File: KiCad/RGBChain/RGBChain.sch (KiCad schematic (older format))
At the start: 72 parts, among them J1 AudioJack2_Ground, J2 SWD, J3 USB_B_Micro, J4 Barrel_Jack, P1 USB_C_Plug_USB2.0, Q1 IRF7404, Q2 SQJB80EP, Q3 IRLML2502, SW1 Rotary_Encoder_Switch, SW2 SW_SPDT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

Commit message: PCB done
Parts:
- removed D6: WS2812B, LED_THT:LED_D5.0mm-4_RGB_Staggered_Pins, symbol LED:WS2812B
- added D6: WS2812D, LED_THT:LED_D5.0mm-4_RGB, symbol myLib:WS2812D
- added D7, D8: RED LED, LED_THT:LED_D3.0mm, symbol Device:LED
- J1: footprint Connector_Audio:Jack_3.5mm_CUI_SJ-3523-SMT_Horizontal -> JPConnectors:Jack_3.5mm_Lumberg_1503_03
- SW2: footprint Button_Switch_THT:SW_E-Switch_EG1224_SPDT_Angled -> JPSwitches:NINIGI_5F_M6
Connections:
- wire segments 224 -> 238
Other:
- note added: "I(d)=16mA*3=48mA"
- moved on the sheet: D3, R1
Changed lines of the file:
@@
 $EndDescr
-$Comp
-L LED:WS2812B D6
-U 1 1 5F8AD20A
-P 14700 4200
-F 0 "D6" H 15044 4246 50  0000 L CNN
-F 1 "WS2812B" H 15044 4155 50  0000 L CNN
-F 2 "LED_THT:LED_D5.0mm-4_RGB_Staggered_Pins" H 14750 3900 50  0001 L TNN
-F 3 "https://cdn-shop.adafruit.com/datasheets/WS2812B.pdf" H 14800 3825 50  0001 L TNN
-	1    14700 4200
-	1    0    0    -1
-$EndComp
 $Comp
 L Device:Battery_Cell BT1
@@
 F 0 "J1" H 14470 3168 50  0000 R CNN
 F 1 "AudioJack2_Ground" H 14470 3077 50  0000 R CNN
-F 2 "Connector_Audio:Jack_3.5mm_CUI_SJ-3523-SMT_Horizontal" H 14650 3150 50  0001 C CNN
+F 2 "JPConnectors:Jack_3.5mm_Lumberg_1503_03" H 14650 3150 50  0001 C CNN
 F 3 "~" H 14650 3150 50  0001 C CNN
 	1    14650 3150
@@
 U 1 1 5F8C9FC5
 P 3650 4150
-F 0 "D2" V 3689 4032 50  0000 R CNN
-F 1 "RED LED" V 3598 4032 50  0000 R CNN
+F 0 "D2" V 3700 4350 50  0000 R CNN
+F 1 "RED LED" V 3600 4550 50  0000 R CNN
 F 2 "LED_SMD:LED_0805_2012Metric" H 3650 4150 50  0001 C CNN
 F 3 "~" H 3650 4150 50  0001 C CNN
@@
 L Device:R R1
 U 1 1 5F8CA8EE
-P 3650 4450
-F 0 "R1" H 3580 4404 50  0000 R CNN
-F 1 "3k3" H 3580 4495 50  0000 R CNN
-F 2 "Resistor_SMD:R_0805_2012Metric" V 3580 4450 50  0001 C CNN
-F 3 "~" H 3650 4450 50  0001 C CNN
-	1    3650 4450
+P 3650 4550
+F 0 "R1" H 3580 4504 50  0000 R CNN
+F 1 "3k3" H 3580 4595 50  0000 R CNN
+F 2 "Resistor_SMD:R_0805_2012Metric" V 3580 4550 50  0001 C CNN
+F 3 "~" H 3650 4550 50  0001 C CNN
+	1    3650 4550
 	-1   0    0    1
 $EndComp
@@
 Connection ~ 3650 3900
 Wire Wire Line
-	3650 3900 4200 3900
+	3650 3900 3800 3900
 $Comp
 L power:VBUS #PWR0103
@@
 L power:GNDPWR #PWR0104
 U 1 1 5F8D62DF
-P 3650 4600
-F 0 "#PWR0104" H 3650 4400 50  0001 C CNN
-F 1 "GNDPWR" H 3654 4446 50  0000 C CNN
-F 2 "" H 3650 4550 50  0001 C CNN
-F 3 "" H 3650 4550 50  0001 C CNN
-	1    3650 4600
+P 3650 4700
+F 0 "#PWR0104" H 3650 4500 50  0001 C CNN
+F 1 "GNDPWR" H 3654 4546 50  0000 C CNN
+F 2 "" H 3650 4650 50  0001 C CNN
+F 3 "" H 3650 4650 50  0001 C CNN
+	1    3650 4700
 	1    0    0    -1
 $EndComp
@@
 L Device:LED D3
 U 1 1 5F8DB333
-P 6400 4800
-F 0 "D3" H 6393 5016 50  0000 C CNN
-F 1 "RED LED" H 6393 4925 50  0000 C CNN
-F 2 "LED_SMD:LED_0805_2012Metric" H 6400 4800 50  0001 C CNN
-F 3 "~" H 6400 4800 50  0001 C CNN
-	1    6400 4800
+P 6500 4800
+F 0 "D3" H 6500 4550 50  0000 C CNN
+F 1 "RED LED" H 6500 4650 50  0000 C CNN
+F 2 "LED_SMD:LED_0805_2012Metric" H 6500 4800 50  0001 C CNN
+F 3 "~" H 6500 4800 50  0001 C CNN
+	1    6500 4800
 	1    0    0    -1
 $EndComp
@@
 L power:VBUS #PWR0108
 U 1 1 5F8DBA77
-P 6550 4800
-F 0 "#PWR0108" H 6550 4650 50  0001 C CNN
-F 1 "VBUS" V 6565 4928 50  0000 L CNN
-F 2 "" H 6550 4800 50  0001 C CNN
-F 3 "" H 6550 4800 50  0001 C CNN
-	1    6550 4800
+P 6750 4800
+F 0 "#PWR0108" H 6750 4650 50  0001 C CNN
+F 1 "VBUS" V 6765 4928 50  0000 L CNN
+F 2 "" H 6750 4800 50  0001 C CNN
+F 3 "" H 6750 4800 50  0001 C CNN
+	1    6750 4800
 	0    1    1    0
 $EndComp
@@
 F 0 "SW2" H 2000 6535 50  0000 C CNN
 F 1 "SW_SPDT" H 2000 6444 50  0000 C CNN
-F 2 "Button_Switch_THT:SW_E-Switch_EG1224_SPDT_Angled" H 2000 6250 50  0001 C CNN
+F 2 "JPSwitches:NINIGI_5F_M6" H 2000 6250 50  0001 C CNN
 F 3 "~" H 2000 6250 50  0001 C CNN
 	1    2000 6250
@@
 Wire Wire Line
 	11600 6000 11450 6000
+$Comp
+L Device:LED D7
+U 1 1 5FF899B0
+P 3800 4150
+F 0 "D7" V 3839 4032 50  0000 R CNN
+F 1 "RED LED" V 3748 4032 50  0000 R CNN
+F 2 "LED_THT:LED_D3.0mm" H 3800 4150 50  0001 C CNN
+F 3 "~" H 3800 4150 50  0001 C CNN
+	1    3800 4150
+	0    -1   -1   0
+$EndComp
+Wire Wire Line
+	3650 4300 3650 4350
+Wire Wire Line
+	3650 4350 3800 4350
+Wire Wire Line
+	3800 4350 3800 4300
+Connection ~ 3650 4350
+Wire Wire Line
+	3650 4350 3650 4400
+Wire Wire Line
+	3800 4000 3800 3900
+Connection ~ 3800 3900
+Wire Wire Line
+	3800 3900 4200 3900
+$Comp
+L Device:LED D8
+U 1 1 5FFDB156
+P 6500 4650
+F 0 "D8" H 6493 4866 50  0000 C CNN
+F 1 "RED LED" H 6493 4775 50  0000 C CNN
+F 2 "LED_THT:LED_D3.0mm" H 6500 4650 50  0001 C CNN
+F 3 "~" H 6500 4650 50  0001 C CNN
+	1    6500 4650
+	1    0    0    -1
+$EndComp
+Wire Wire Line
+	6250 4800 6300 4800
+Wire Wire Line
+	6300 4800 6300 4650
+Wire Wire Line
+	6300 4650 6350 4650
+Connection ~ 6300 4800
+Wire Wire Line
+	6300 4800 6350 4800
+Wire Wire Line
+	6650 4650 6700 4650
+Wire Wire Line
+	6700 4650 6700 4800
+Wire Wire Line
+	6700 4800 6650 4800
+Wire Wire Line
+	6700 4800 6750 4800
+Connection ~ 6700 4800
+Text Notes 14600 4850 0    50   ~ 0
+I(d)=16mA*3=48mA
+$Comp
+L myLib:WS2812D D6
+U 1 1 6008788C
+P 14700 4200
+F 0 "D6" H 15044 4246 50  0000 L CNN
+F 1 "WS2812D" H 15044 4155 50  0000 L CNN
+F 2 "LED_THT:LED_D5.0mm-4_RGB" H 14750 3900 50  0001 L TNN
+F 3 "https://cdn-shop.adafruit.com/datasheets/WS2812B.pdf" H 14800 3825 50  0001 L TNN
+	1    14700 4200
+	1    0    0    -1
+$EndComp
 $EndSCHEMATC

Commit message: PCB more work
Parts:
- removed JP1: 0, Jumper:SolderJumper-2_P1.3mm_Bridged_Pad1.0x1.5mm, symbol Device:Jumper_NC_Small
- BT1, BT2, BT3: footprint Battery:BatteryHolder_Keystone_1042_1x18650 -> JPConnectors:BatteryHolder_Keystone_1042_1x18650
- R10, R4: footprint Resistor_SMD:R_0805_2012Metric -> Resistor_SMD:R_0603_1608Metric
- U5: value STM32L051K8Tx -> STM32L051K8T6
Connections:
- wire segments 238 -> 242
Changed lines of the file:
@@
 F 0 "BT1" H 3200 1650 50  0000 L CNN
 F 1 "Li-Ion" H 2900 1850 50  0000 L CNN
-F 2 "Battery:BatteryHolder_Keystone_1042_1x18650" V 3150 1760 50  0001 C CNN
+F 2 "JPConnectors:BatteryHolder_Keystone_1042_1x18650" V 3150 1760 50  0001 C CNN
 F 3 "~" V 3150 1760 50  0001 C CNN
 	1    3150 1700
@@
 F 0 "BT2" H 3550 1650 50  0000 L CNN
 F 1 "Li-Ion" H 3250 1850 50  0000 L CNN
-F 2 "Battery:BatteryHolder_Keystone_1042_1x18650" V 3500 1760 50  0001 C CNN
+F 2 "JPConnectors:BatteryHolder_Keystone_1042_1x18650" V 3500 1760 50  0001 C CNN
 F 3 "~" V 3500 1760 50  0001 C CNN
 	1    3500 1700
@@
 F 0 "BT3" H 3900 1650 50  0000 L CNN
 F 1 "Li-Ion" H 3600 1850 50  0000 L CNN
-F 2 "Battery:BatteryHolder_Keystone_1042_1x18650" V 3850 1760 50  0001 C CNN
+F 2 "JPConnectors:BatteryHolder_Keystone_1042_1x18650" V 3850 1760 50  0001 C CNN
 F 3 "~" V 3850 1760 50  0001 C CNN
 	1    3850 1700
@@
 F 0 "R4" V 4493 4950 50  0000 C CNN
 F 1 "100k" V 4584 4950 50  0000 C CNN
-F 2 "Resistor_SMD:R_0805_2012Metric" V 4630 4950 50  0001 C CNN
+F 2 "Resistor_SMD:R_0603_1608Metric" V 4630 4950 50  0001 C CNN
 F 3 "~" H 4700 4950 50  0001 C CNN
 	1    4700 4950
@@
 	2250 7650 2250 7500
 $Comp
-L Device:Jumper_NC_Small JP1
-U 1 1 5F8F644E
-P 1750 8150
-F 0 "JP1" H 1750 8362 50  0000 C CNN
-F 1 "0" H 1750 8271 50  0000 C CNN
-F 2 "Jumper:SolderJumper-2_P1.3mm_Bridged_Pad1.0x1.5mm" H 1750 8150 50  0001 C CNN
-F 3 "~" H 1750 8150 50  0001 C CNN
-	1    1750 8150
-	1    0    0    -1
-$EndComp
-$Comp
 L power:GNDPWR #PWR0116
 U 1 1 5F8F6DD7
@@
 L power:GND #PWR0117
 U 1 1 5F8F777D
-P 1850 8150
-F 0 "#PWR0117" H 1850 7900 50  0001 C CNN
-F 1 "GND" V 1855 8022 50  0000 R CNN
-F 2 "" H 1850 8150 50  0001 C CNN
-F 3 "" H 1850 8150 50  0001 C CNN
-	1    1850 8150
+P 1650 8150
+F 0 "#PWR0117" H 1650 7900 50  0001 C CNN
+F 1 "GND" V 1655 8022 50  0000 R CNN
+F 2 "" H 1650 8150 50  0001 C CNN
+F 3 "" H 1650 8150 50  0001 C CNN
+	1    1650 8150
 	0    -1   -1   0
 $EndComp
-Wire Wire Line
-	1750 7500 1750 7650
 $Comp
 L Device:C C13
@@
 F 0 "R10" H 13420 4396 50  0000 L CNN
 F 1 "100k" H 13420 4305 50  0000 L CNN
-F 2 "Resistor_SMD:R_0805_2012Metric" V 13280 4350 50  0001 C CNN
+F 2 "Resistor_SMD:R_0603_1608Metric" V 13280 4350 50  0001 C CNN
 F 3 "~" H 13350 4350 50  0001 C CNN
 	1    13350 4350
@@
 P 10950 5200
 F 0 "U5" H 11050 4100 50  0000 C CNN
-F 1 "STM32L051K8Tx" H 11300 4200 50  0000 C CNN
+F 1 "STM32L051K8T6" H 11300 4200 50  0000 C CNN
 F 2 "Package_QFP:LQFP-32_7x7mm_P0.8mm" H 10450 4300 50  0001 R CNN
 F 3 "http://www.st.com/st-web-ui/static/active/en/resource/technical/document/datasheet/DM00108219.pdf" H 10950 5200 50  0001 C CNN
@@
 	1    0    0    -1
 $EndComp
+Wire Wire Line
+	1700 7500 1700 7550
+Wire Wire Line
+	1700 7550 1750 7550
+Wire Wire Line
+	1800 7550 1800 7500
+Wire Wire Line
+	1750 7650 1750 7550
+Connection ~ 1750 7550
+Wire Wire Line
+	1750 7550 1800 7550
 $EndSCHEMATC

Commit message: Last pcb changes
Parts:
- removed J2: SWD, Connector_PinHeader_2.54mm:PinHeader_1x06_P2.54mm_Vertical, symbol Connector_Generic:Conn_01x06
- added J2: SWD, Connector_PinHeader_2.54mm:PinHeader_1x05_P2.54mm_Vertical, symbol Connector_Generic:Conn_01x05
- J4: value Barrel_Jack -> Power
- P1: footprint Connector_USB:USB_C_Receptacle_Amphenol_12401610E4-2A -> JPConnectors:USB_C_Receptacle_Adam_Tech
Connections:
- net +3V3: now also J2.1 (Pin_1)
- net GND: now also J2.3 (Pin_3)
- net NRST: now also J2.5 (Pin_5)
- net SWCLK: now also J2.2 (Pin_2)
- net SWDIO: now also J2.4 (Pin_4)
- net VBUS: no longer D3.2 (A), D8.2 (A)
- net at C2.1, D1.1 (K), D2.2 (A)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: now also D3.2 (A), D8.2 (A)
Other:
- note added: "I(led)=16mA*3=48mA"
- note removed: "I(d)=16mA*3=48mA"
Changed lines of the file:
@@
-$EndComp
-$Comp
-L Connector_Generic:Conn_01x06 J2
-U 1 1 5F8AFA1F
-P 14300 5750
-F 0 "J2" H 14380 5742 50  0000 L CNN
-F 1 "SWD" H 14380 5651 50  0000 L CNN
-F 2 "Connector_PinHeader_2.54mm:PinHeader_1x06_P2.54mm_Vertical" H 14300 5750 50  0001 C CNN
-F 3 "~" H 14300 5750 50  0001 C CNN
-	1    14300 5750
-	1    0    0    -1
 $EndComp
 $Comp
@@
 Connection ~ 4500 4650
 Wire Wire Line
-	4500 4650 4500 3900
+	4500 4650 4500 4150
 Wire Wire Line
 	4850 3900 5150 3900
@@
 	1    0    0    -1
 $EndComp
-$Comp
-L power:VBUS #PWR0108
-U 1 1 5F8DBA77
-P 6750 4800
-F 0 "#PWR0108" H 6750 4650 50  0001 C CNN
-F 1 "VBUS" V 6765 4928 50  0000 L CNN
-F 2 "" H 6750 4800 50  0001 C CNN
-F 3 "" H 6750 4800 50  0001 C CNN
-	1    6750 4800
-	0    1    1    0
-$EndComp
 Wire Wire Line
 	5950 4800 5700 4800
@@
 Text GLabel 13950 5950 0    50   Input ~ 0
 NRST
-Text GLabel 13950 6050 0    50   Input ~ 0
-SWO
-Wire Wire Line
-	13950 6050 14100 6050
 Wire Wire Line
 	13950 5950 14100 5950
@@
 F 0 "P1" H 1207 2617 50  0000 C CNN
 F 1 "USB_C_Plug_USB2.0" H 1207 2526 50  0000 C CNN
-F 2 "Connector_USB:USB_C_Receptacle_Amphenol_12401610E4-2A" H 1250 1750 50  0001 C CNN
+F 2 "JPConnectors:USB_C_Receptacle_Adam_Tech" H 1250 1750 50  0001 C CNN
 F 3 "https://www.usb.org/sites/default/files/documents/usb_type-c.zip" H 1250 1750 50  0001 C CNN
 	1    1100 1750
@@
 P 1000 4400
 F 0 "J4" H 1057 4725 50  0000 C CNN
-F 1 "Barrel_Jack" H 1057 4634 50  0000 C CNN
+F 1 "Power" H 1057 4634 50  0000 C CNN
 F 2 "JPConnectors:PowerSocketSMD" H 1050 4360 50  0001 C CNN
 F 3 "~" H 1050 4360 50  0001 C CNN
@@
 Wire Wire Line
 	6700 4800 6650 4800
-Wire Wire Line
-	6700 4800 6750 4800
-Connection ~ 6700 4800
 Text Notes 14600 4850 0    50   ~ 0
-I(d)=16mA*3=48mA
+I(led)=16mA*3=48mA
 $Comp
 L myLib:WS2812D D6
@@
 Wire Wire Line
 	1750 7550 1800 7550
+$Comp
+L Connector_Generic:Conn_01x05 J2
+U 1 1 5FA56BB8
+P 14300 5750
+F 0 "J2" H 14380 5792 50  0000 L CNN
+F 1 "SWD" H 14380 5701 50  0000 L CNN
+F 2 "Connector_PinHeader_2.54mm:PinHeader_1x05_P2.54mm_Vertical" H 14300 5750 50  0001 C CNN
+F 3 "~" H 14300 5750 50  0001 C CNN
+	1    14300 5750
+	1    0    0    -1
+$EndComp
+Wire Wire Line
+	6700 4650 6700 4150
+Wire Wire Line
+	6700 4150 4500 4150
+Connection ~ 6700 4650
+Connection ~ 4500 4150
+Wire Wire Line
+	4500 4150 4500 3900
 $EndSCHEMATC

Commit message: Single colour effect implemented
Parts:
- Q1: value IRF7404 -> IRF7204
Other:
- note added: "Bugs:\nPower led is on even when not chargin"
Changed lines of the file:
@@
 P 5450 4000
 F 0 "Q1" V 5792 4000 50  0000 C CNN
-F 1 "IRF7404" V 5701 4000 50  0000 C CNN
+F 1 "IRF7204" V 5701 4000 50  0000 C CNN
 F 2 "Package_SO:SOIC-8_3.9x4.9mm_P1.27mm" H 5650 3925 50  0001 L CIN
 F 3 "http://www.infineon.com/dgdl/irf7404.pdf?fileId=5546d462533600a4015355fa2b5b1b9e" V 5450 4000 50  0001 L CNN
@@
 Wire Wire Line
 	4500 4150 4500 3900
+Text Notes -1700 3450 0    50   ~ 0
+Bugs:\nPower led is on even when not chargin
 $EndSCHEMATC

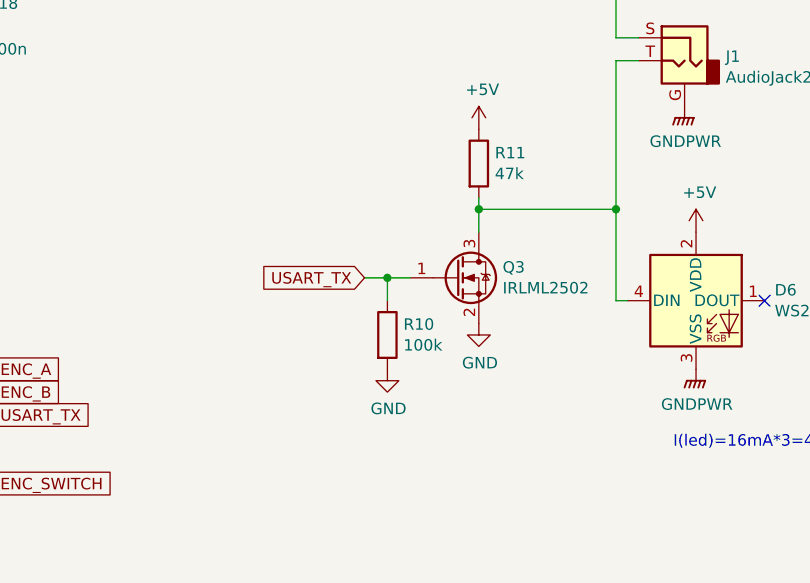
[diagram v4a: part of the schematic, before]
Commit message: More work on effects
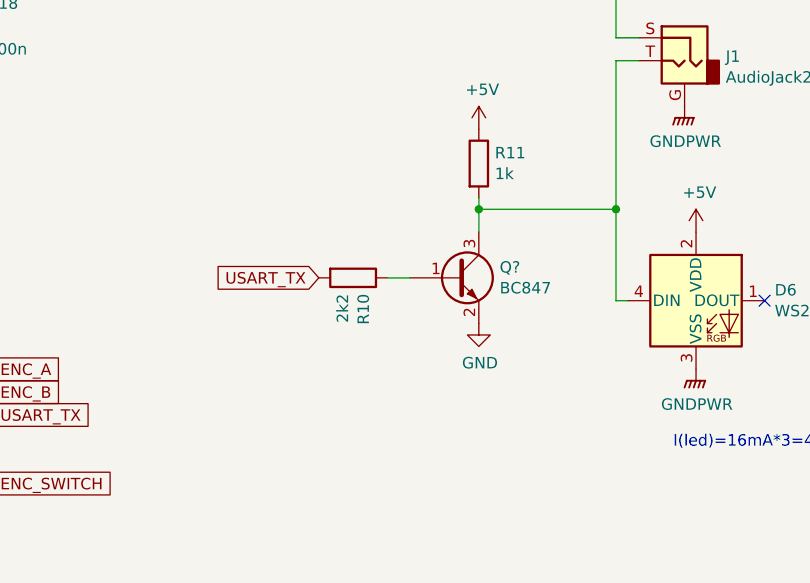
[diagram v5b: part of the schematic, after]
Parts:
- removed Q3: IRLML2502, Package_TO_SOT_SMD:SOT-23, symbol Transistor_FET:IRLML2060
- added Q?: BC847, Package_TO_SOT_SMD:SOT-23, symbol Transistor_BJT:BC847
- R10: value 100k -> 2k2
- R11: value 47k -> 1k
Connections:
- net GND: now also Q?.2 (E); no longer R10.2
- net USART_TX: now also R10.2; no longer R10.1
- net at D6.4 (DIN), J1.T, R11.2: now also Q?.3 (C)
- new net: Q?.1 (B), R10.1
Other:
- moved on the sheet: R10
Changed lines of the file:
@@
 	1    0    0    -1
 $EndComp
-Text GLabel 13250 4100 0    50   Input ~ 0
+Text GLabel 13050 4100 0    50   Input ~ 0
 USART_TX
 $Comp
@@
 https://webench.ti.com/power-designer/switching-regulator/customize/12?AppType=None&Flavor=None&O1I=0.4&O1V=5.0&Topology=Boost&VinMax=5.0&VinMin=3&VoltageOption=None&base_pn=LM2735Y&flavor=None&lang_chosen=en_US&op_TA=30&optfactor=3&origin=ti_search
 $Comp
-L Transistor_FET:IRLML2060 Q3
-U 1 1 5FAC3A29
-P 13650 4100
-F 0 "Q3" H 13854 4146 50  0000 L CNN
-F 1 "IRLML2502" H 13854 4055 50  0000 L CNN
-F 2 "Package_TO_SOT_SMD:SOT-23" H 13850 4025 50  0001 L CIN
-F 3 "https://www.infineon.com/dgdl/irlml2060pbf.pdf?fileId=5546d462533600a401535664b7fb25ee" H 13650 4100 50  0001 L CNN
-	1    13650 4100
-	1    0    0    -1
-$EndComp
-$Comp
 L power:GND #PWR0144
 U 1 1 5FAC7F38
@@
 P 13750 3600
 F 0 "R11" H 13820 3646 50  0000 L CNN
-F 1 "47k" H 13820 3555 50  0000 L CNN
+F 1 "1k" H 13820 3555 50  0000 L CNN
 F 2 "Resistor_SMD:R_0805_2012Metric" V 13680 3600 50  0001 C CNN
 F 3 "~" H 13750 3600 50  0001 C CNN
@@
 L Device:R R10
 U 1 1 5FAFCC1F
-P 13350 4350
-F 0 "R10" H 13420 4396 50  0000 L CNN
-F 1 "100k" H 13420 4305 50  0000 L CNN
-F 2 "Resistor_SMD:R_0603_1608Metric" V 13280 4350 50  0001 C CNN
-F 3 "~" H 13350 4350 50  0001 C CNN
-	1    13350 4350
-	1    0    0    -1
-$EndComp
-Wire Wire Line
-	13250 4100 13350 4100
-Wire Wire Line
-	13350 4100 13350 4200
-Connection ~ 13350 4100
+P 13200 4100
+F 0 "R10" H 13270 4146 50  0000 L CNN
+F 1 "2k2" H 13270 4055 50  0000 L CNN
+F 2 "Resistor_SMD:R_0603_1608Metric" V 13130 4100 50  0001 C CNN
+F 3 "~" H 13200 4100 50  0001 C CNN
+	1    13200 4100
+	0    1    1    0
+$EndComp
 Wire Wire Line
 	13350 4100 13450 4100
-$Comp
-L power:GND #PWR0146
-U 1 1 5FB0BAE2
-P 13350 4500
-F 0 "#PWR0146" H 13350 4250 50  0001 C CNN
-F 1 "GND" H 13355 4327 50  0000 C CNN
-F 2 "" H 13350 4500 50  0001 C CNN
-F 3 "" H 13350 4500 50  0001 C CNN
-	1    13350 4500
-	1    0    0    -1
-$EndComp
 Wire Wire Line
 	14350 3150 14350 3800
@@
 Text Notes -1700 3450 0    50   ~ 0
 Bugs:\nPower led is on even when not chargin
+$Comp
+L Transistor_BJT:BC847 Q?
+U 1 1 5FD00BD5
+P 13650 4100
+F 0 "Q?" H 13841 4146 50  0000 L CNN
+F 1 "BC847" H 13841 4055 50  0000 L CNN
+F 2 "Package_TO_SOT_SMD:SOT-23" H 13850 4025 50  0001 L CIN
+F 3 "http://www.infineon.com/dgdl/Infineon-BC847SERIES_BC848SERIES_BC849SERIES_BC850SERIES-DS-v01_01-en.pdf?fileId=db3a304314dca389011541d4630a1657" H 13650 4100 50  0001 L CNN
+	1    13650 4100
+	1    0    0    -1
+$EndComp
 $EndSCHEMATC

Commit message: More effects. Refactoring
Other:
- note added: "Bugs:\nPower led is on even when not chargin\nLevel converter too slow - UART speed set to 800k but should be 2400k"
- note removed: "Bugs:\nPower led is on even when not chargin"
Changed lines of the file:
@@
 Wire Wire Line
 	4500 4150 4500 3900
-Text Notes -1700 3450 0    50   ~ 0
-Bugs:\nPower led is on even when not chargin
+Text Notes -2900 3600 0    50   ~ 0
+Bugs:\nPower led is on even when not chargin\nLevel converter too slow - UART speed set to 800k but should be 2400k
 $Comp
 L Transistor_BJT:BC847 Q?
